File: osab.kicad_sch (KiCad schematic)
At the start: 88 parts, among them CON1 TF-01A, CON2 PJ-3420-A-SMT, CON3 TYPE-C-31-M-12, Q1 BC847B, SW1 PPP, SW10 RESET, SW2 VOL-, SW3 VOL+, SW4 CHAP-, SW5 CHAP+, SW6 OT/NT, SW7 BOOK-, SW8 BOOK+, SW9 BUTTON_LOCK, U1 VS1000, U2 ME6211C33M5G-N, U3 CAT25640, U4 TP4055, U5 MF5853CS, U6 PAM8302AAS, Y1 12MHz

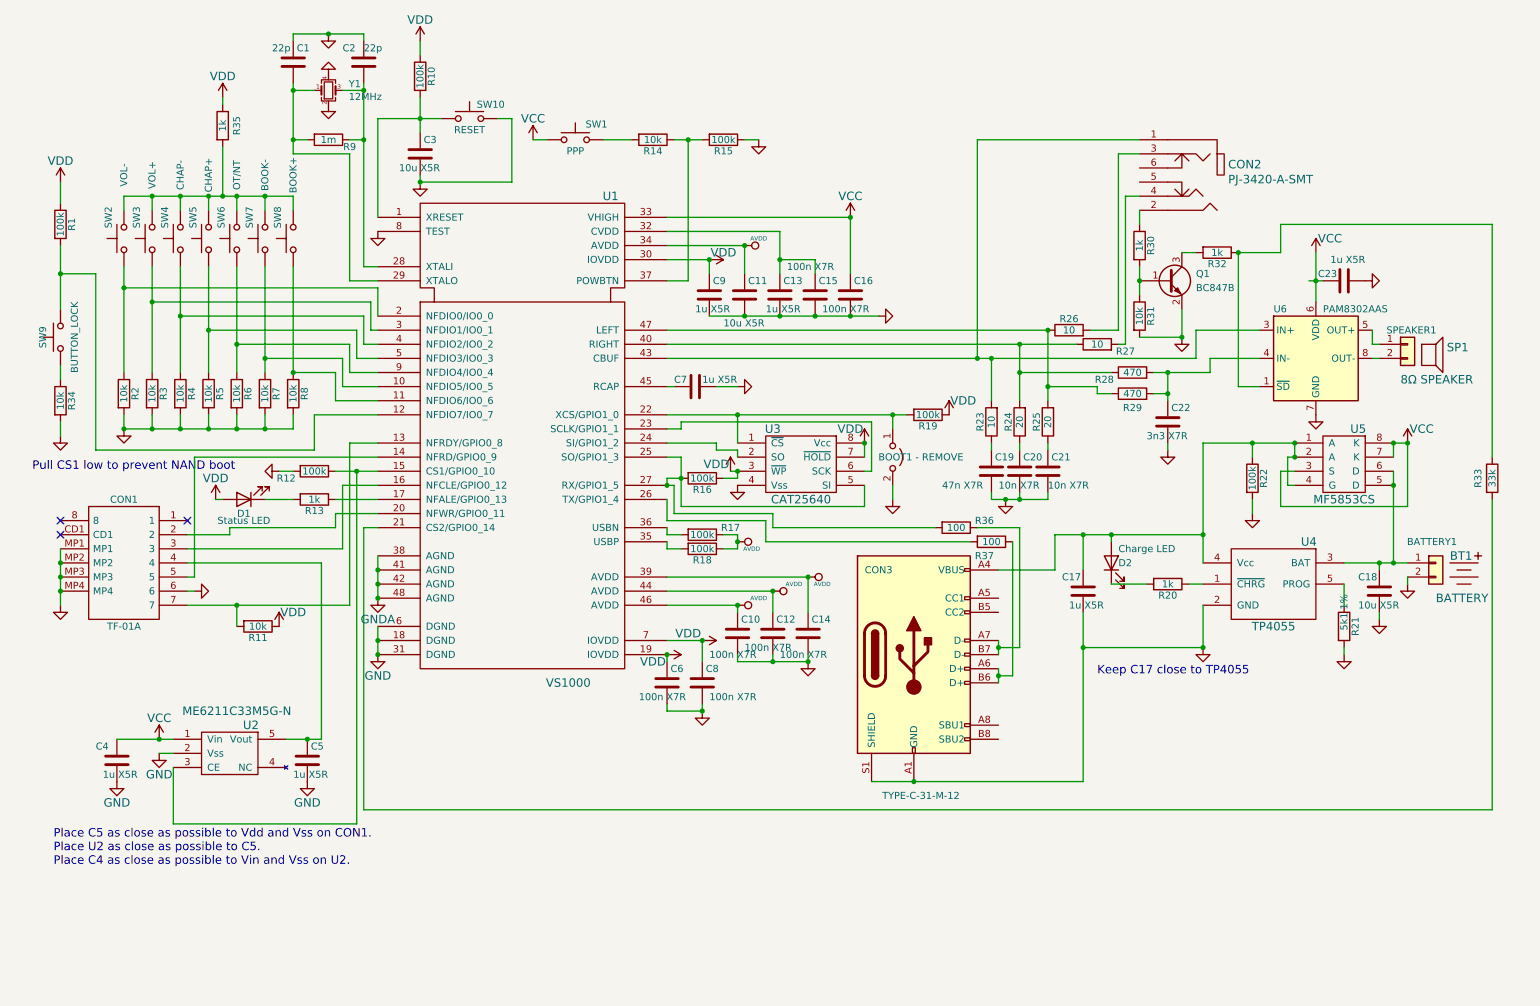
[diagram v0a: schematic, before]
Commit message: production: Torch; ferrite beads
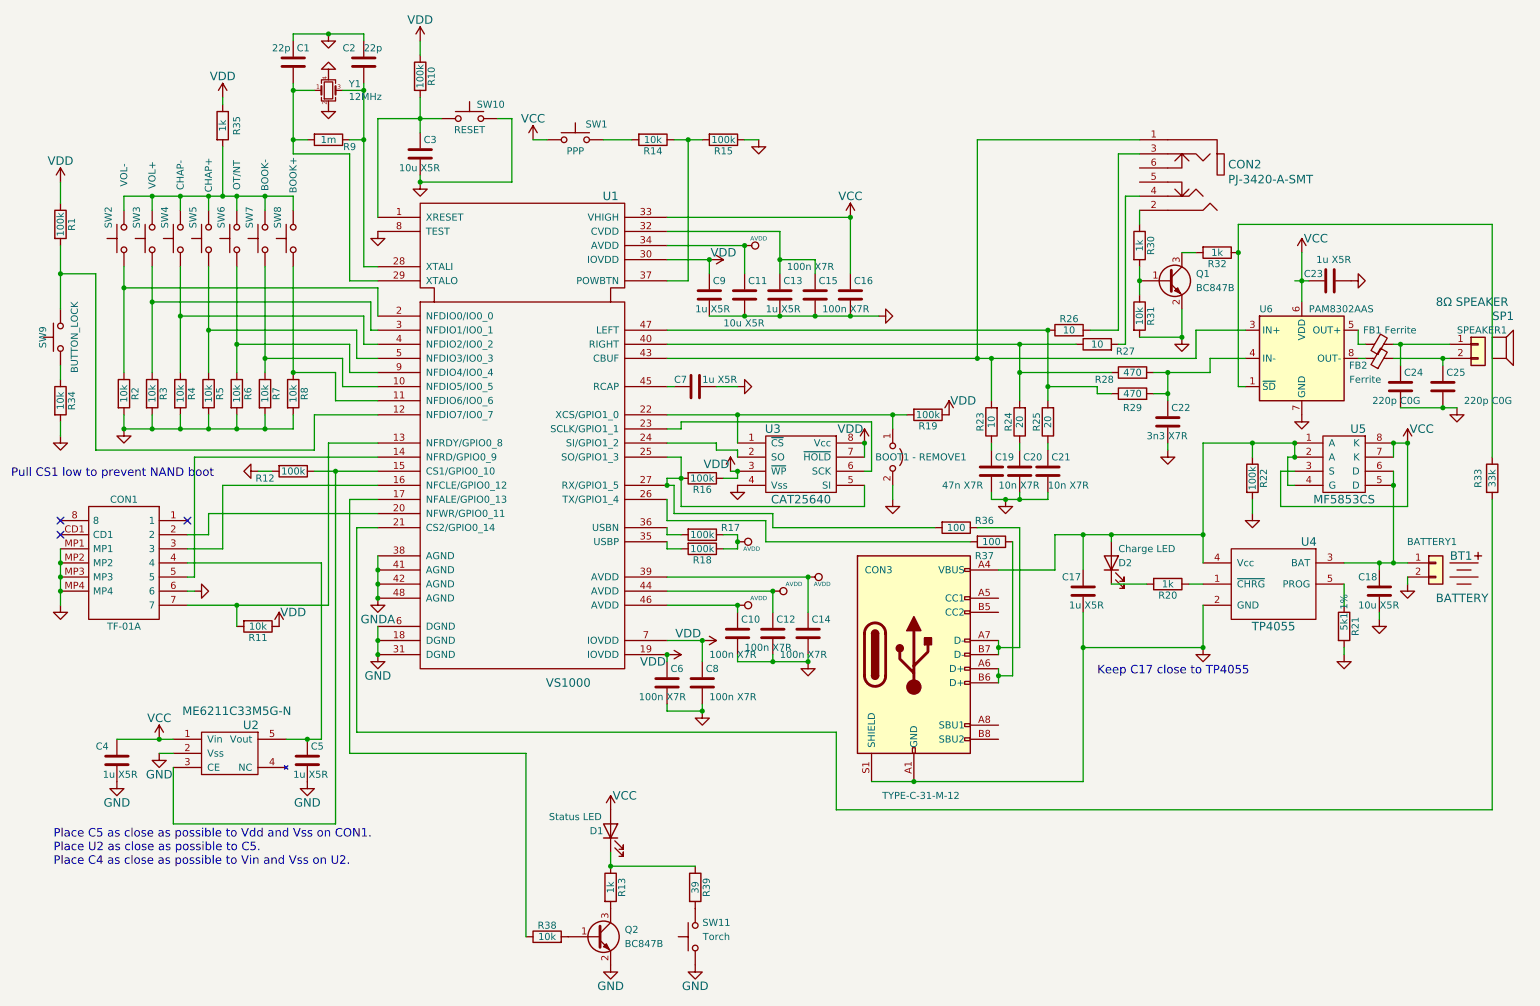
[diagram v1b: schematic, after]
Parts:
- added C24, C25: 220p C0G, Capacitor_SMD:C_0603_1608Metric, symbol Device:C
- added FB1, FB2: Ferrite, Resistor_SMD:R_0603_1608Metric, symbol Device:FerriteBead_Small
- added Q2: BC847B, Package_TO_SOT_SMD:SOT-23, symbol Transistor_BJT:BC850
- added R38: 10k, Resistor_SMD:R_0603_1608Metric, symbol Device:R
- added R39: 39, Resistor_SMD:R_0603_1608Metric, symbol Device:R
- added SW11: Torch, Button_Switch_SMD:SW_SPST_TL3342, symbol Switch:SW_Push
- BOOT1 - REMOVE1: renamed from BOOT1 - REMOVE
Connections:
- net GND: now also C24.2, C25.2, Q2.2 (E), SW11.1
- net VCC: now also D1.2 (A)
- net VDD: no longer D1.2 (A)
- net at U1.17 (NFALE/GPIO0_13): now also R38.1; no longer R13.1
- net at D1.1 (K): now also R13.1, R39.1; no longer R13.2
- net at SPEAKER1.1 (Pin_1): now also C24.1, FB1.2; no longer U6.5 (OUT+)
- net at SPEAKER1.2 (Pin_2): now also C25.1, FB2.2; no longer U6.8 (OUT-)
- new net: Q2.3 (C), R13.2
- new net: FB2.1, U6.8 (OUT-)
- new net: R39.2, SW11.2
- new net: Q2.1 (B), R38.2
- new net: FB1.1, U6.5 (OUT+)
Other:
- moved on the sheet: C23, D1, R12, R13, SP1, SPEAKER1, U6

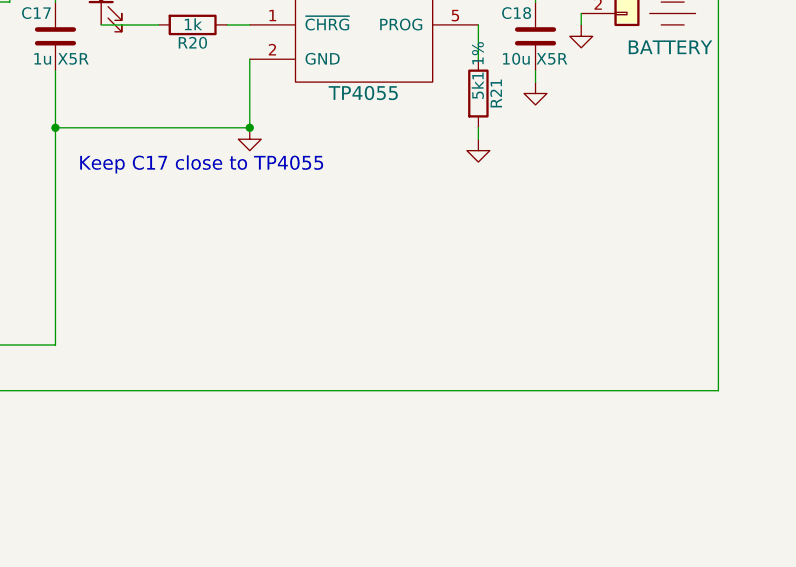
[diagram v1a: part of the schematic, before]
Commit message: production: Added alternate battery
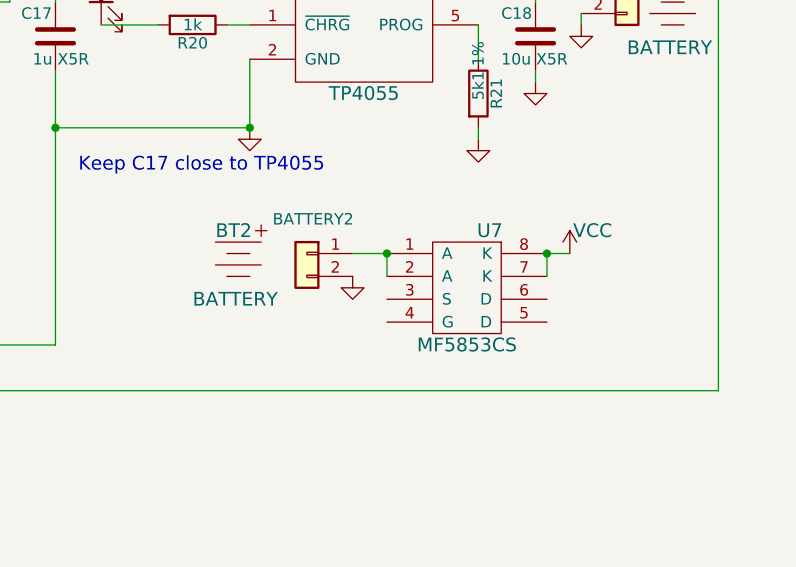
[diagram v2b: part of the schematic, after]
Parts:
- added BATTERY2: Conn_01x02, EasyEDA model, symbol Connector_Generic:Conn_01x02
- added BT2: BATTERY, OSAB:NULL, symbol osab:BATTERY
- added U7: MF5853CS, OSAB:DFN8-2x3-0.65pitch, symbol osab:PJ5853
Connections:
- net GND: now also BATTERY2.2 (Pin_2)
- net VCC: now also U7.7 (K), U7.8 (K)
- new net: BATTERY2.1 (Pin_1), U7.1 (A), U7.2 (A)
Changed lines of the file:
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@@
   (title_block
     (title "OSAB - the Open Source Audio Bible player")
-    (date "2022-03-06")
+    (date "2022-03-07")
     (rev "7")
     (company "theaudiobible.org")
@@
   (junction (at 243.84 96.52) (diameter 0) (color 0 0 0 0)
   )
+  (junction (at 242.57 147.32) (diameter 0) (color 0 0 0 0)
+  )
   (junction (at 220.98 87.63) (diameter 0) (color 0 0 0 0)
   )
@@
   (junction (at 38.1 71.12) (diameter 0) (color 0 0 0 0)
   )
+  (junction (at 260.35 147.32) (diameter 0) (color 0 0 0 0)
+  )
   (junction (at 227.33 113.03) (diameter 0) (color 0 0 0 0)
   )
@@
     (stroke (width 0) (type default) (color 0 0 0 0))
   )
+  (wire (pts (xy 238.76 147.32) (xy 242.57 147.32))
+    (stroke (width 0) (type default) (color 0 0 0 0))
+  )
   (wire (pts (xy 132.08 109.22) (xy 149.86 109.22))
     (stroke (width 0) (type default) (color 0 0 0 0))
@@
     (stroke (width 0) (type default) (color 0 0 0 0))
   )
+  (wire (pts (xy 260.35 147.32) (xy 260.35 149.86))
+    (stroke (width 0) (type default) (color 0 0 0 0))
+  )
   (wire (pts (xy 236.22 106.68) (xy 236.22 109.22))
     (stroke (width 0) (type default) (color 0 0 0 0))
@@
     (stroke (width 0) (type default) (color 0 0 0 0))
   )
+  (wire (pts (xy 260.35 147.32) (xy 262.89 147.32))
+    (stroke (width 0) (type default) (color 0 0 0 0))
+  )
   (wire (pts (xy 76.2 73.66) (xy 43.18 73.66))
     (stroke (width 0) (type default) (color 0 0 0 0))
@@
     (stroke (width 0) (type default) (color 0 0 0 0))
   )
+  (wire (pts (xy 242.57 147.32) (xy 242.57 149.86))
+    (stroke (width 0) (type default) (color 0 0 0 0))
+  )
   (wire (pts (xy 144.78 41.91) (xy 147.32 41.91))
     (stroke (width 0) (type default) (color 0 0 0 0))
@@
     (pin "2")
   )
+  (symbol (lib_id "Connector_Generic:Conn_01x02") (at 233.68 147.32 0) (mirror y) (unit 1)
+    (in_bom yes) (on_board yes)
+    (property "Reference" "BATTERY2" (id 0) (at 229.87 143.51 0)
+      (effects (font (size 1.27 1.27)) (justify right))
+    )
+    (property "Value" "Conn_01x02" (id 1) (at 231.648 149.8346 0)
+      (effects (font (size 1.27 1.27)) (justify left) hide)
+    )
+    (property "Footprint" "EasyEDA model" (id 2) (at 233.68 147.32 0)
+      (effects (font (size 1.27 1.27)) hide)
+    )
+    (property "Datasheet" "https://datasheet.lcsc.com/lcsc/2009131405_CAX-XH-2PWB_C722862.pdf" (id 3) (at 233.68 147.32 0)
+      (effects (font (size 1.27 1.27)) hide)
+    )
+    (property "3D-model" "Included in KiCad" (id 4) (at 233.68 147.32 0)
+      (effects (font (size 1.27 1.27)) hide)
+    )
+    (property "Link" "https://lcsc.com/product-detail/Wire-To-Board-Wire-To-Wire-Connector_CAX-XH-2PWB_C722862.html" (id 5) (at 233.68 147.32 0)
+      (effects (font (size 1.27 1.27)) hide)
+    )
+    (property "MPN" "XH-2PWB" (id 6) (at 233.68 147.32 0)
+      (effects (font (size 1.27 1.27)) hide)
+    )
+    (pin "1")
+    (pin "2")
+  )
+  (symbol (lib_id "power:GND") (at 238.76 149.86 0) (unit 1)
+    (in_bom yes) (on_board yes)
+    (property "Reference" "#PWR055" (id 0) (at 238.76 156.21 0)
+      (effects (font (size 1.524 1.524)) hide)
+    )
+    (property "Value" "GND" (id 1) (at 238.76 153.67 0)
+      (effects (font (size 1.524 1.524)) hide)
+    )
+    (property "Footprint" "" (id 2) (at 238.76 149.86 0)
+      (effects (font (size 1.524 1.524)))
+    )
+    (property "Datasheet" "" (id 3) (at 238.76 149.86 0)
+      (effects (font (size 1.524 1.524)))
+    )
+    (pin "1")
+  )
   (symbol (lib_id "Transistor_BJT:BC850") (at 118.11 185.42 0) (unit 1)
     (in_bom yes) (on_board yes)
@@
     (pin "3")
   )
+  (symbol (lib_id "power:VCC") (at 262.89 147.32 0) (unit 1)
+    (in_bom yes) (on_board yes)
+    (property "Reference" "#PWR056" (id 0) (at 262.89 151.13 0)
+      (effects (font (size 1.524 1.524)) hide)
+    )
+    (property "Value" "VCC" (id 1) (at 265.43 144.78 0)
+      (effects (font (size 1.524 1.524)))
+    )
+    (property "Footprint" "" (id 2) (at 262.89 147.32 0)
+      (effects (font (size 1.524 1.524)))
+    )
+    (property "Datasheet" "" (id 3) (at 262.89 147.32 0)
+      (effects (font (size 1.524 1.524)))
+    )
+    (pin "1")
+  )
   (symbol (lib_id "Device:C") (at 262.89 86.36 0) (unit 1)
     (in_bom yes) (on_board yes)
@@
     (pin "2")
   )
+  (symbol (lib_id "osab:BATTERY") (at 226.06 143.51 0) (unit 1)
+    (in_bom yes) (on_board yes)
+    (property "Reference" "BT2" (id 0) (at 223.52 144.78 0)
+      (effects (font (size 1.524 1.524)) (justify left))
+    )
+    (property "Value" "BATTERY" (id 1) (at 220.98 152.4 0)
+      (effects (font (size 1.524 1.524)) (justify left))
+    )
+    (property "Footprint" "OSAB:NULL" (id 2) (at 226.06 143.51 0)
+      (effects (font (size 1.524 1.524)) hide)
+    )
+    (property "Datasheet" "" (id 3) (at 226.06 143.51 0)
+      (effects (font (size 1.524 1.524)) hide)
+    )
+  )
   (symbol (lib_id "Switch:SW_Push") (at 135.89 185.42 90) (unit 1)
     (in_bom yes) (on_board yes)
@@
     (pin "2")
   )
+  (symbol (lib_id "osab:PJ5853") (at 251.46 148.59 0) (unit 1)
+    (in_bom yes) (on_board yes)
+    (property "Reference" "U7" (id 0) (at 254 144.78 0)
+      (effects (font (size 1.524 1.524)))
+    )
+    (property "Value" "MF5853CS" (id 1) (at 251.46 157.48 0)
+      (effects (font (size 1.524 1.524)))
+    )
+    (property "Footprint" "OSAB:DFN8-2x3-0.65pitch" (id 2) (at 251.46 144.78 0)
+      (effects (font (size 1.524 1.524)) hide)
+    )
+    (property "Datasheet" "https://datasheet.lcsc.com/szlcsc/1910111742_Megapower-MF5853CS_C375698.pdf" (id 3) (at 251.46 144.78 0)
+      (effects (font (size 1.524 1.524)) hide)
+    )
+    (property "Link" "https://lcsc.com/product-detail/Others_Megapower-MF5853CS_C375698.html" (id 4) (at 251.46 148.59 0)
+      (effects (font (size 1.27 1.27)) hide)
+    )
+    (property "MPN" "MF5853CS" (id 5) (at 251.46 148.59 0)
+      (effects (font (size 1.27 1.27)) hide)
+    )
+    (property "3D-model" "May need to make a footprint?" (id 6) (at 251.46 148.59 0)
+      (effects (font (size 1.27 1.27)) hide)
+    )
+    (pin "1")
+    (pin "2")
+    (pin "3")
+    (pin "4")
+    (pin "5")
+    (pin "6")
+    (pin "7")
+    (pin "8")
+  )
   (symbol (lib_id "Device:FerriteBead_Small") (at 259.08 78.74 90) (unit 1)
     (in_bom yes) (on_board yes)
@@
       (reference "#PWR054") (unit 1) (value "GND") (footprint "")
     )
+    (path "/7f631368-8068-416b-b649-0c5fea39375c"
+      (reference "#PWR055") (unit 1) (value "GND") (footprint "")
+    )
+    (path "/b877890a-8080-4d73-9dae-3ad60bc85007"
+      (reference "#PWR056") (unit 1) (value "VCC") (footprint "")
+    )
     (path "/00000000-0000-0000-0000-00005e19fe42"
       (reference "#PWR0101") (unit 1) (value "GND") (footprint "")
@@
       (reference "BATTERY1") (unit 1) (value "Conn_01x02") (footprint "EasyEDA model")
     )
+    (path "/697c6cc9-d8aa-43e6-9910-d8f7a42cad10"
+      (reference "BATTERY2") (unit 1) (value "Conn_01x02") (footprint "EasyEDA model")
+    )
     (path "/00000000-0000-0000-0000-000054d41aff"
       (reference "BOOT1 - REMOVE1") (unit 1) (value "BOOT") (footprint "OSAB:Terminals_2_SMD")
@@
       (reference "BT1") (unit 1) (value "BATTERY") (footprint "OSAB:NULL")
     )
+    (path "/d4833389-5c8d-4d68-83d7-5ccb30223098"
+      (reference "BT2") (unit 1) (value "BATTERY") (footprint "OSAB:NULL")
+    )
     (path "/00000000-0000-0000-0000-00005808fac7"
       (reference "C1") (unit 1) (value "22p") (footprint "Capacitor_SMD:C_0603_1608Metric")
@@
       (reference "U6") (unit 1) (value "PAM8302AAS") (footprint "Package_SO:MSOP-8_3x3mm_P0.65mm")
     )
+    (path "/de84cf5c-224e-4bc1-ad7d-c71908826f3a"
+      (reference "U7") (unit 1) (value "MF5853CS") (footprint "OSAB:DFN8-2x3-0.65pitch")
+    )
     (path "/00000000-0000-0000-0000-00005e12ed4a"
